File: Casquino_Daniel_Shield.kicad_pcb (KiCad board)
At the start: 2 copper layers, 101.6 x 53.3 mm, 13 parts, among them J1 Power, J2 PWM, J3 Analog, J4 PWM, J5 Analog, J6 Communication, J7 Digital

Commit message: footprint finished
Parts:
- added BZ1: Buzzer, Buzzer_Beeper:Buzzer_12x9.5RM7.6, F.Cu at (67.9, 81.9)
- added D1: LED, LED_THT:LED_D5.0mm, F.Cu at (47.7, 53.2)
- added D2: LED, LED_THT:LED_D5.0mm, F.Cu at (47.7, 60.7)
- added D3: LED, LED_THT:LED_D5.0mm, F.Cu at (47.7, 68.2)
- added D4: LED, LED_THT:LED_D5.0mm, F.Cu at (47.7, 75.6)
- added DHT11: Conn_01x03_Socket, Connector_PinSocket_2.54mm:PinSocket_1x03_P2.54mm_Vertical, F.Cu at (47.6, 81.7)
- added D_BUZZER1: 1N4148, Diode_THT:D_DO-35_SOD27_P7.62mm_Horizontal, F.Cu at (64.9, 66.3)
- added I2C1: Conn_01x04, Connector_Molex:Molex_KK-254_AE-6410-04A_1x04_P2.54mm_Vertical, F.Cu at (55.0, 79.1)
- added J8: Screw_Terminal_01x02, TerminalBlock_Phoenix:TerminalBlock_Phoenix_MKDS-1,5-2-5.08_1x02_P5.08mm_Horizontal, F.Cu at (68.5, 94.9)
- added LDR1: A1050, OptoDevice:R_LDR_D6.4mm_P3.4mm_Vertical, F.Cu at (55.1, 94.9)
- added RV1: POT, Potentiometer_THT:Potentiometer_Alps_RK09L_Single_Vertical, F.Cu at (65.0, 54.5)
- added R_BUZZER1: 1k, Resistor_THT:R_Axial_DIN0207_L6.3mm_D2.5mm_P7.62mm_Horizontal, F.Cu at (36.1, 51.5)
- added R_LDR1: 10k, Resistor_THT:R_Axial_DIN0207_L6.3mm_D2.5mm_P7.62mm_Horizontal, F.Cu at (36.1, 55.6)
- added R_LED1: 330, Resistor_THT:R_Axial_DIN0207_L6.3mm_D2.5mm_P7.62mm_Horizontal, F.Cu at (36.1, 59.6)
- added R_LED2: 330, Resistor_THT:R_Axial_DIN0207_L6.3mm_D2.5mm_P7.62mm_Horizontal, F.Cu at (36.1, 63.7)
- added R_LED3: 330, Resistor_THT:R_Axial_DIN0207_L6.3mm_D2.5mm_P7.62mm_Horizontal, F.Cu at (36.1, 67.7)
- added R_LED4: 330, Resistor_THT:R_Axial_DIN0207_L6.3mm_D2.5mm_P7.62mm_Horizontal, F.Cu at (36.1, 71.8)
- added R_SW1: 10k, Resistor_THT:R_Axial_DIN0207_L6.3mm_D2.5mm_P7.62mm_Horizontal, F.Cu at (36.1, 75.8)
- added R_SW2: 10k, Resistor_THT:R_Axial_DIN0207_L6.3mm_D2.5mm_P7.62mm_Horizontal, F.Cu at (36.1, 79.9)
- added R_SW_RESET1: 10k, Resistor_THT:R_Axial_DIN0207_L6.3mm_D2.5mm_P7.62mm_Horizontal, F.Cu at (36.1, 83.9)
- added SW1: SW_Push, Button_Switch_THT:SW_PUSH_6mm, F.Cu at (54.8, 51.5)
- added SW2: SW_Push, Button_Switch_THT:SW_PUSH_6mm, F.Cu at (54.8, 60.1)
- added SW_RESET1: SW_Push, Button_Switch_THT:SW_PUSH_6mm, F.Cu at (54.8, 68.6)
- added T_BUZZER1: S8050, Package_TO_SOT_THT:TO-92_Inline, F.Cu at (47.3, 92.3)
- added UART1: Conn_01x04, Connector_Molex:Molex_KK-254_AE-6410-04A_1x04_P2.54mm_Vertical, F.Cu at (55.0, 86.9)

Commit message: pcb wip
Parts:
- moved R_LED1 142.5 mm to (178.5, 54.5), turned to -90 degrees
- moved R_LED3 142.5 mm to (178.5, 65.0), turned to -90 degrees
- moved D3 138.8 mm to (186.5, 72.0), turned to 180 degrees
- moved D4 138.8 mm to (186.5, 79.5), turned to 180 degrees
- moved D2 138.8 mm to (186.5, 64.5), turned to 180 degrees
- moved D1 138.8 mm to (186.5, 57.0), turned to 180 degrees
- moved DHT11 138.3 mm to (185.5, 91.5), turned to 180 degrees
- moved R_LED2 137.2 mm to (173.0, 54.5), turned to -90 degrees
- moved R_LED4 137.1 mm to (173.0, 65.0), turned to -90 degrees
- moved UART1 116.4 mm to (171.4, 91.0)
- moved I2C1 111.9 mm to (166.9, 83.0)
- moved R_BUZZER1 110.0 mm to (145.9, 57.5)
- moved R_LDR1 102.7 mm to (133.5, 88.0), turned to 180 degrees
- moved T_BUZZER1 98.2 mm to (140.0, 60.0)
- moved RV1 90.5 mm to (150.5, 84.2)
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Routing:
- net +5V: track 0.00 -> 178.4 mm
- net GND: track 0.00 -> 119.8 mm
- net VCC: track 0.00 -> 45.6 mm
- net /22: track 0.00 -> 40.7 mm
- net /*4: track 0.00 -> 31.7 mm
- net Net-(BZ1--): track 0.00 -> 29.1 mm
- net /*5: track 0.00 -> 28.7 mm
- net /*2: track 0.00 -> 22.3 mm
- net /A0: track 0.00 -> 21.2 mm
- net /*3: track 0.00 -> 19.3 mm
- net Net-(D4-A): track 0.00 -> 13.8 mm
- net /A1: track 0.00 -> 12.1 mm
- net Net-(D2-A): track 0.00 -> 11.9 mm
- net Net-(D1-A): track 0.00 -> 9.05 mm
- net Net-(T_BUZZER1-B): track 0.00 -> 6.36 mm
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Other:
- board text added: "BajadorDePepa2560"

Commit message: todo fix drc
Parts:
- RV1: footprint Potentiometer_THT:Potentiometer_Alps_RK09L_Single_Vertical -> Potentiometer_THT:Potentiometer_Bourns_3386P_Vertical
- moved UART1 56.2 mm to (125.9, 58.0)
- moved I2C1 43.4 mm to (126.2, 68.0)
- moved DHT11 16.6 mm to (170.0, 85.5), turned to 90 degrees
- moved D1 5.53 mm to (186.5, 62.5)
- moved D2 5.53 mm to (186.5, 70.0)
- moved D3 5.53 mm to (186.5, 77.5)
- moved D4 5.53 mm to (186.5, 85.0)
- moved R_LED1 5.53 mm to (178.5, 60.0)
- moved R_LED2 5.53 mm to (173.0, 60.0)
- moved R_LED3 5.53 mm to (178.5, 70.5)
- moved R_LED4 5.53 mm to (173.0, 70.5)
- moved RV1 2.06 mm to (152.4, 85.0), turned to -90 degrees
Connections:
- R_BUZZER1 pad 2: /D6 -> /*6
- R_SW1 pad 1: /D18 -> /TX1/18
- R_SW2 pad 1: /D19 -> /RX1/19
- SW1 pad 2: /D18 -> /TX1/18
- SW2 pad 2: /D19 -> /RX1/19
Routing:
- net /TX1/18: track 0.00 -> 78.8 mm
- net GND: track 119.8 -> 185.7 mm
- net /SCL/21: track 0.00 -> 65.4 mm
- net /SDA/20: track 0.00 -> 65.4 mm
- net /~{RESET}: track 3.71 -> 41.2 mm
- net +5V: track 178.4 -> 210.5 mm
- net /RX1/19: track 0.00 -> 26.1 mm
- net /22: track 40.7 -> 60.1 mm
- net /*6: track 0.00 -> 10.5 mm
- net /*5: track 28.7 -> 34.7 mm
- net /*4: track 31.7 -> 37.5 mm
- net /D19: track 3.71 -> 0.00 mm
- net /D18: track 3.71 -> 0.00 mm
- net /*2: track 22.3 -> 24.6 mm
- net /*3: track 19.3 -> 21.6 mm
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
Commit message: fixed schem erc errors
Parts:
- moved D1 1.53 mm to (186.5, 61.0)
- moved D2 1.03 mm to (186.5, 69.0)
- moved SW1 1.00 mm to (110.0, 59.0)
- moved D3 0.53 mm to (186.5, 77.0)
- moved SW2 0.50 mm to (110.0, 68.0)
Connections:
- I2C1 pad 1: /D20 -> /SDA/20
- I2C1 pad 2: /D21 -> /SCL/21
- UART1 pad 1: /D18 -> /TX1/18
- UART1 pad 2: /D19 -> /RX1/19
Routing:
- net GND: track 185.7 -> 191.5 mm
- net Net-(D1-A): track 9.05 -> 10.9 mm
- net /*6: track 10.5 -> 11.6 mm
- net /~{RESET}: track 41.2 -> 40.3 mm
- net +5V: track 210.5 -> 209.9 mm

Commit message: unfucked pcb
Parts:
- moved SW2 82.6 mm to (188.8, 93.0)
- moved SW1 76.7 mm to (178.8, 93.0)
- moved R_SW1 73.6 mm to (181.6, 83.8)
- moved R_SW2 69.9 mm to (181.6, 78.8)
- moved I2C1 62.0 mm to (186.8, 54.5), turned to -90 degrees
- moved D4 56.7 mm to (134.0, 63.5), turned to -90 degrees
- moved UART1 52.4 mm to (178.2, 54.5), turned to -90 degrees
- moved D3 46.5 mm to (142.0, 63.5), turned to -90 degrees
- moved BZ1 40.9 mm to (113.4, 60.8), turned to 0 degrees
- moved D2 36.9 mm to (150.0, 63.5), turned to -90 degrees
- moved R_LED3 31.7 mm to (152.2, 52.8)
- moved R_LED4 31.1 mm to (147.5, 52.8)
- moved D_BUZZER1 29.6 mm to (118.4, 73.8), turned to 0 degrees
- moved D1 28.6 mm to (158.0, 63.5), turned to -90 degrees
- moved R_SW_RESET1 27.6 mm to (132.9, 93.5)
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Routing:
- net /SDA/20: track 65.4 -> 6.51 mm
- net /SCL/21: track 65.4 -> 9.24 mm
- net /22: track 60.1 -> 21.6 mm
- net /*4: track 37.5 -> 4.00 mm
- net /TX1/18: track 78.9 -> 48.5 mm
- net /*5: track 34.7 -> 4.92 mm
- net /~{RESET}: track 40.3 -> 14.5 mm
- net /RX1/19: track 26.5 -> 50.7 mm
- net +5V: track 209.9 -> 188.9 mm
- net /*2: track 24.6 -> 4.93 mm
- net /*3: track 21.6 -> 4.01 mm
- net VCC: track 45.6 -> 57.4 mm
- net /*6: track 11.6 -> 0.00 mm
- net Net-(D3-A): track 5.94 -> 12.6 mm
- net GND: track 191.5 -> 195.3 mm
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- added copper zone on B.Cu, net GND
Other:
- board text added: "SubidorDePepa2560"
- board text removed: "BajadorDePepa2560"
- board text removed: "ICSP"

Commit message: tweaked some connections
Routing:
- net /*6: track 0.00 -> 7.88 mm
- net +5V: track 188.9 -> 192.6 mm
- net VCC: track 57.4 -> 58.1 mm
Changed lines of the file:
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@@
 	)
 	(segment
-		(start 140.122233 98.71)
-		(end 141.157767 98.71)
+		(start 139.35 98.71)
+		(end 143.697767 98.71)
 		(width 0.4)
 		(layer "B.Cu")
@@
 	)
 	(segment
-		(start 141.157767 98.71)
-		(end 141.93 97.937767)
-		(width 0.4)
-		(layer "B.Cu")
-		(net "+5V")
-	)
-	(segment
 		(start 191 56.75)
 		(end 191 52.18)
@@
 	)
 	(segment
+		(start 156.42 86.25)
+		(end 157.54 87.37)
+		(width 0.4)
+		(layer "B.Cu")
+		(net "+5V")
+	)
+	(segment
+		(start 166.62 87.37)
+		(end 172.25 93)
+		(width 0.4)
+		(layer "B.Cu")
+		(net "+5V")
+	)
+	(segment
+		(start 103.75 85)
+		(end 103.75 82.75)
+		(width 0.4)
+		(layer "B.Cu")
+		(net "+5V")
+	)
+	(segment
+		(start 105 81.5)
+		(end 110.69 81.5)
+		(width 0.4)
+		(layer "B.Cu")
+		(net "+5V")
+	)
+	(segment
+		(start 189.25 68.5)
+		(end 191 66.75)
+		(width 0.4)
+		(layer "B.Cu")
+		(net "+5V")
+	)
+	(segment
+		(start 138.1 97.46)
+		(end 139.35 98.71)
+		(width 0.4)
+		(layer "B.Cu")
+		(net "+5V")
+	)
+	(segment
+		(start 138.1 97.46)
+		(end 138.1 90.35)
+		(width 0.4)
+		(layer "B.Cu")
+		(net "+5V")
+	)
+	(segment
+		(start 138.1 90.35)
+		(end 134.5 86.75)
+		(width 0.4)
+		(layer "B.Cu")
+		(net "+5V")
+	)
+	(segment
+		(start 144.47 93.857057)
+		(end 145.35 92.977057)
+		(width 0.4)
+		(layer "B.Cu")
+		(net "+5V")
+	)
+	(segment
+		(start 110.69 81.5)
+		(end 115.97 76.22)
+		(width 0.4)
+		(layer "B.Cu")
+		(net "+5V")
+	)
+	(segment
+		(start 143.697767 98.71)
+		(end 144.47 97.937767)
+		(width 0.4)
+		(layer "B.Cu")
+		(net "+5V")
+	)
+	(segment
+		(start 145.35 89.35)
+		(end 145.35 86.25)
+		(width 0.4)
+		(layer "B.Cu")
+		(net "+5V")
+	)
+	(segment
+		(start 115.97 76.22)
+		(end 118.44 73.75)
+		(width 0.4)
+		(layer "B.Cu")
+		(net "+5V")
+	)
+	(segment
+		(start 182.25 93)
+		(end 180 90.75)
+		(width 0.4)
+		(layer "B.Cu")
+		(net "+5V")
+	)
+	(segment
+		(start 180 90.75)
+		(end 178.75 90.75)
+		(width 0.4)
+		(layer "B.Cu")
+		(net "+5V")
+	)
+	(segment
+		(start 188.5 68.5)
+		(end 189.25 68.5)
+		(width 0.4)
+		(layer "B.Cu")
+		(net "+5V")
+	)
+	(segment
+		(start 188.92 59.58)
+		(end 186.75 59.58)
+		(width 0.4)
+		(layer "B.Cu")
+		(net "+5V")
+	)
+	(segment
 		(start 174.5 90.75)
 		(end 172.25 93)
@@
 	)
 	(segment
-		(start 156.42 86.25)
-		(end 157.54 87.37)
-		(width 0.4)
-		(layer "B.Cu")
-		(net "+5V")
-	)
-	(segment
-		(start 166.62 87.37)
-		(end 172.25 93)
-		(width 0.4)
-		(layer "B.Cu")
-		(net "+5V")
-	)
-	(segment
-		(start 103.75 85)
-		(end 103.75 82.75)
-		(width 0.4)
-		(layer "B.Cu")
-		(net "+5V")
-	)
-	(segment
-		(start 105 81.5)
-		(end 110.69 81.5)
-		(width 0.4)
-		(layer "B.Cu")
-		(net "+5V")
-	)
-	(segment
-		(start 141.93 96.397057)
-		(end 145.35 92.977057)
-		(width 0.4)
-		(layer "B.Cu")
-		(net "+5V")
-	)
-	(segment
-		(start 189.25 68.5)
-		(end 191 66.75)
-		(width 0.4)
-		(layer "B.Cu")
-		(net "+5V")
-	)
-	(segment
-		(start 138.1 97.46)
-		(end 138.1 90.35)
-		(width 0.4)
-		(layer "B.Cu")
-		(net "+5V")
-	)
-	(segment
-		(start 141.93 97.937767)
-		(end 141.93 96.397057)
-		(width 0.4)
-		(layer "B.Cu")
-		(net "+5V")
-	)
-	(segment
-		(start 138.1 90.35)
-		(end 134.5 86.75)
-		(width 0.4)
-		(layer "B.Cu")
-		(net "+5V")
-	)
-	(segment
-		(start 110.69 81.5)
-		(end 115.97 76.22)
-		(width 0.4)
-		(layer "B.Cu")
-		(net "+5V")
-	)
-	(segment
-		(start 145.35 89.35)
-		(end 145.35 86.25)
-		(width 0.4)
-		(layer "B.Cu")
-		(net "+5V")
-	)
-	(segment
-		(start 115.97 76.22)
-		(end 118.44 73.75)
-		(width 0.4)
-		(layer "B.Cu")
-		(net "+5V")
-	)
-	(segment
-		(start 180 90.75)
-		(end 174.5 90.75)
-		(width 0.4)
-		(layer "B.Cu")
-		(net "+5V")
-	)
-	(segment
-		(start 188.5 68.5)
-		(end 189.25 68.5)
-		(width 0.4)
-		(layer "B.Cu")
-		(net "+5V")
-	)
-	(segment
-		(start 188.92 59.58)
-		(end 186.75 59.58)
+		(start 178.75 93)
+		(end 178.75 90.75)
 		(width 0.4)
 		(layer "B.Cu")
@@
 	)
 	(segment
+		(start 178.75 90.75)
+		(end 174.5 90.75)
+		(width 0.4)
+		(layer "B.Cu")
+		(net "+5V")
+	)
+	(segment
 		(start 191 56.75)
 		(end 191 57.5)
@@
 	)
 	(segment
-		(start 138.1 97.46)
-		(end 138.872233 97.46)
-		(width 0.4)
-		(layer "B.Cu")
-		(net "+5V")
-	)
-	(segment
-		(start 138.872233 97.46)
-		(end 140.122233 98.71)
-		(width 0.4)
-		(layer "B.Cu")
-		(net "+5V")
-	)
-	(segment
 		(start 145.25 84)
 		(end 154.17 84)
@@
 	)
 	(segment
-		(start 182.25 93)
-		(end 180 90.75)
-		(width 0.4)
-		(layer "B.Cu")
-		(net "+5V")
-	)
-	(segment
 		(start 113.4 60.75)
 		(end 113.4 73.65)
@@
 	)
 	(segment
+		(start 144.47 97.937767)
+		(end 144.47 93.857057)
+		(width 0.4)
+		(layer "B.Cu")
+		(net "+5V")
+	)
+	(segment
 		(start 135.75 92)
 		(end 135.75 94.73)
@@
 	)
 	(segment
+		(start 102.75 81.92)
+		(end 102.75 85.75)
+		(width 0.4)
+		(layer "B.Cu")
+		(net "VCC")
+	)
+	(segment
+		(start 145.72 98.68)
+		(end 145.72 97.46)
+		(width 0.4)
+		(layer "B.Cu")
+		(net "VCC")
+	)
+	(segment
+		(start 126.06 99.31)
+		(end 145.09 99.31)
+		(width 0.4)
+		(layer "B.Cu")
+		(net "VCC")
+	)
+	(segment
+		(start 111.75 94.75)
+		(end 121.5 94.75)
+		(width 0.4)
+		(layer "B.Cu")
+		(net "VCC")
+	)
+	(segment
 		(start 105.75 78.92)
 		(end 102.75 81.92)
@@
 	)
 	(segment
-		(start 143.87 99.31)
-		(end 145.72 97.46)
+		(start 102.75 85.75)
+		(end 111.75 94.75)
+		(width 0.4)
+		(layer "B.Cu")
+		(net "VCC")
+	)
+	(segment
+		(start 145.09 99.31)
+		(end 145.72 98.68)
 		(width 0.4)
 		(layer "B.Cu")
@@
 	)
 	(segment
-		(start 102.75 81.92)
-		(end 102.75 85.75)
-		(width 0.4)
-		(layer "B.Cu")
-		(net "VCC")
-	)
-	(segment
-		(start 102.75 85.75)
-		(end 111.75 94.75)
-		(width 0.4)
-		(layer "B.Cu")
-		(net "VCC")
-	)
-	(segment
-		(start 111.75 94.75)
-		(end 121.5 94.75)
-		(width 0.4)
-		(layer "B.Cu")
-		(net "VCC")
-	)
-	(segment
-		(start 126.06 99.31)
-		(end 143.87 99.31)
-		(width 0.4)
-		(layer "B.Cu")
-		(net "VCC")
-	)
-	(segment
 		(start 150.75 90.75)
 		(end 148.75 88.75)
@@
 	)
 	(segment
+		(start 143.46 54)
+		(end 148.26 49.2)
+		(width 0.4)
+		(layer "B.Cu")
+		(net "/*6")
+	)
+	(segment
+		(start 142.37 54)
+		(end 143.46 54)
+		(width 0.4)
+		(layer "B.Cu")
+		(net "/*6")
+	)
+	(segment

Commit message: fixed template footprints
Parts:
- moved SW_RESET1 7.91 mm to (140.0, 88.5), turned to 180 degrees
- moved D2 3.36 mm to (152.1, 66.1), turned to 90 degrees
- moved D1 3.34 mm to (160.1, 66.1), turned to 90 degrees
- moved D3 3.34 mm to (144.1, 66.1), turned to 90 degrees
- moved D4 3.34 mm to (136.1, 66.1), turned to 90 degrees
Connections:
- J1 pad 6: GND -> (no net)
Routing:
- net GND: track 195.3 -> 0.00 mm
- net +5V: track 192.6 -> 207.3 mm
- net /~{RESET}: track 14.5 -> 25.7 mm
- net /TX1/18: track 48.5 -> 55.0 mm
- net /RX1/19: track 50.7 -> 57.2 mm
- net Net-(D1-A): track 7.22 -> 3.93 mm
- net Net-(D4-A): track 15.8 -> 12.8 mm
- net Net-(D3-A): track 12.6 -> 9.54 mm
- net Net-(D2-A): track 9.34 -> 6.29 mm
- net Net-(BZ1--): track 26.6 -> 25.4 mm
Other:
- outline, holes or cut-outs redrawn

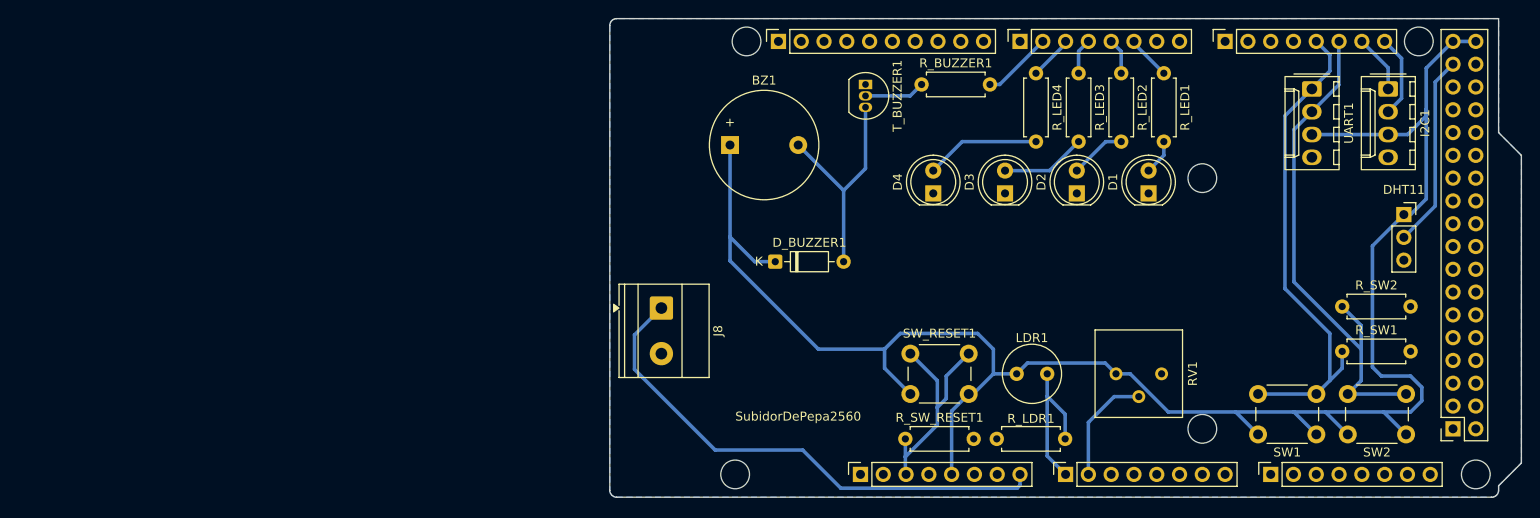
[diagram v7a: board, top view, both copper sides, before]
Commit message: fixed gnd island
placed correct socket footprints
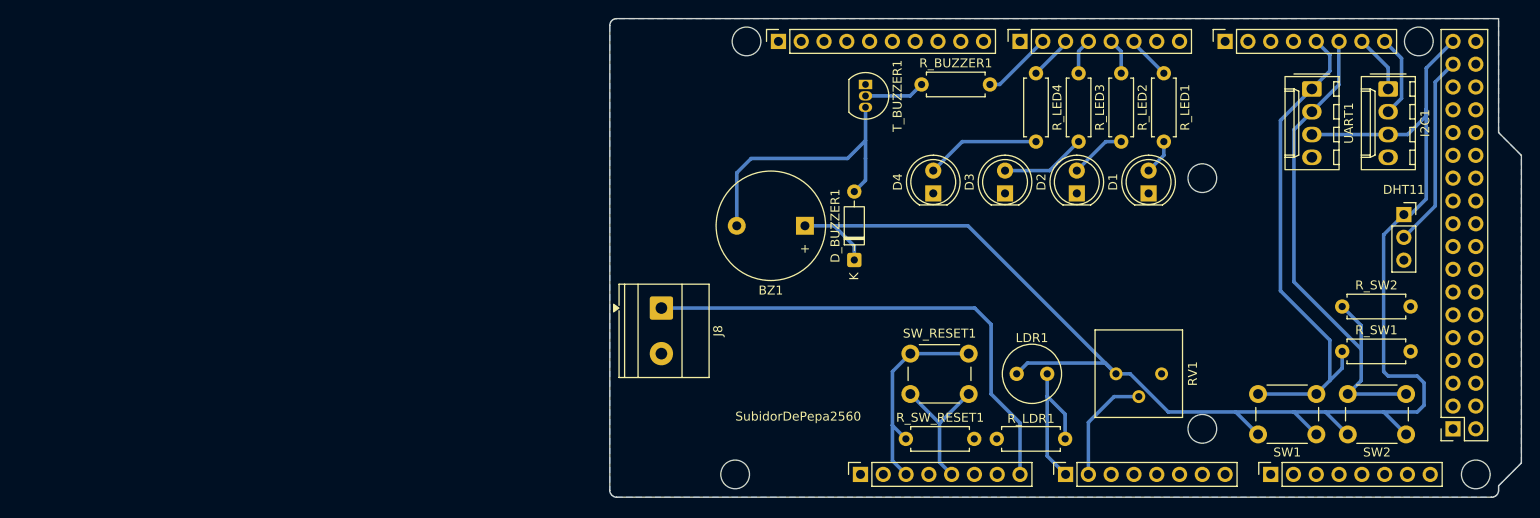
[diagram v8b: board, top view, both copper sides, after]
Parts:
- moved BZ1 12.3 mm to (121.8, 69.8), turned to 180 degrees
- moved D_BUZZER1 8.81 mm to (127.2, 73.6), turned to 90 degrees
- moved R_SW_RESET1 0.06 mm to (133.0, 93.5)
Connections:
- J1 pad 6: (no net) -> unconnected-(J1-Pin_6-Pad6)
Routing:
- net +5V: track 207.3 -> 187.1 mm
- net Net-(BZ1--): track 25.4 -> 31.7 mm
- net VCC: track 57.9 -> 55.6 mm
- net /~{RESET}: track 25.7 -> 23.6 mm
